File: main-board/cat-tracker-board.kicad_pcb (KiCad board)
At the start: 2 copper layers, 69.5 x 29 mm, 40 parts, among them J1 Conn_01x10, J2 USB_C_Receptacle_USB2.0, J3 Conn_01x03, J4 Conn_01x02, Q1 SI3443DDV-T1-GE3, Q2 Q_PNP_BCE, Q3 Q_NPN_BCE, Q4 SI3443DDV-T1-GE3, Q5 SI3443DDV-T1-GE3, U1 ATSAMD21E18A-A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

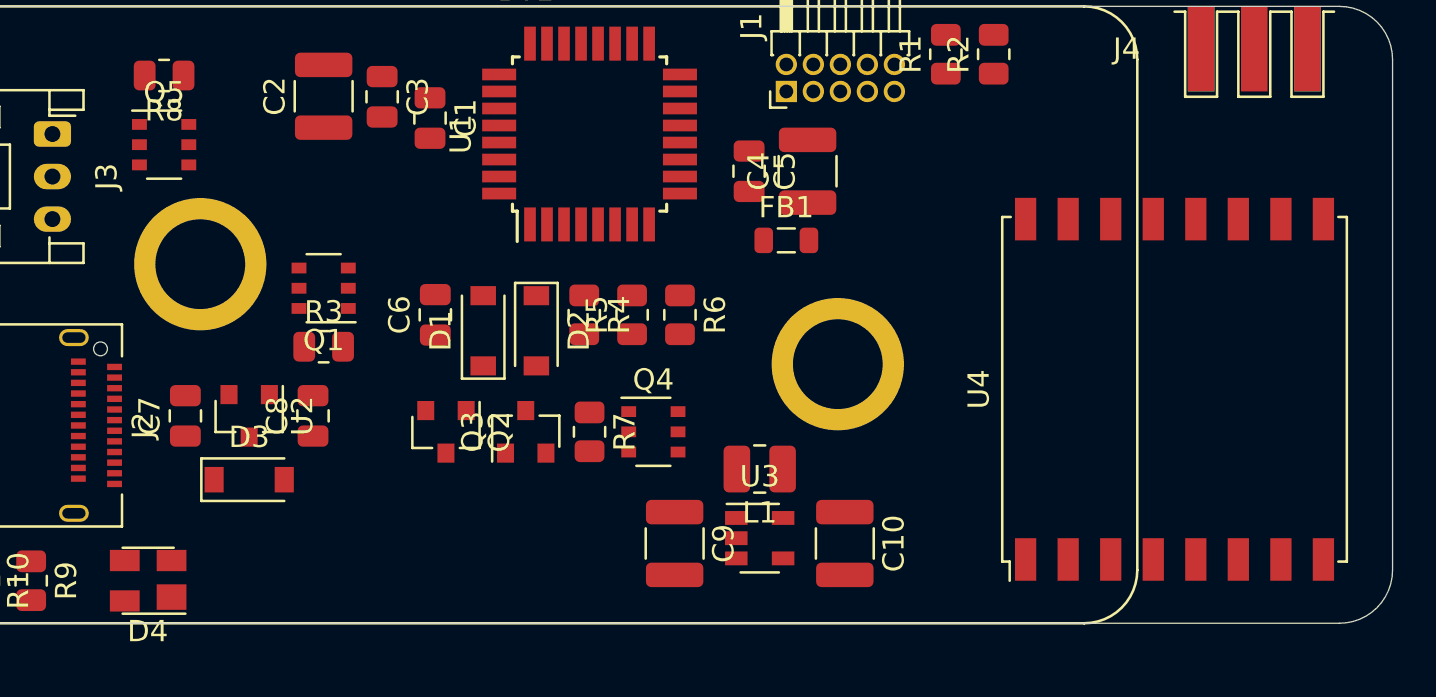
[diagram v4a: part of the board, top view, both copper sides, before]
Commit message: Added zip tie slots.
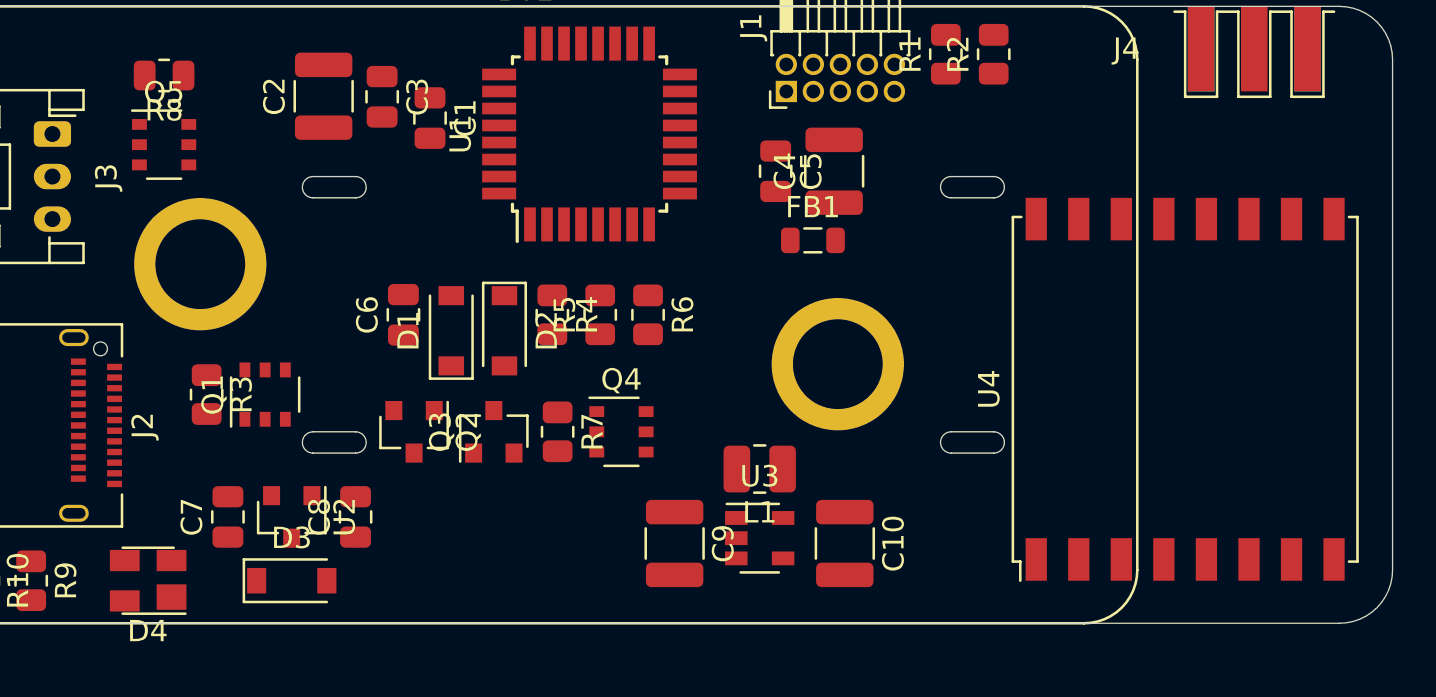
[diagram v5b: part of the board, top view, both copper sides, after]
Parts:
- moved R3 5.94 mm to (13.8, 18.2), turned to 270 degrees
- moved Q1 5.71 mm to (16.5, 18.2), turned to 90 degrees
- moved C7 5.15 mm to (14.8, 24.0)
- moved C8 5.15 mm to (20.8, 24.0)
- moved D3 5.15 mm to (17.8, 27.0)
- moved U2 5.15 mm to (17.8, 24.0)
- moved C6 1.50 mm to (23.0, 14.5)
- moved D1 1.50 mm to (25.2, 15.2)
- moved D2 1.50 mm to (27.8, 15.2)
- moved Q2 1.50 mm to (23.5, 20.0)
- moved Q3 1.50 mm to (27.2, 20.0)
- moved Q4 1.50 mm to (33.2, 20.0)
- moved R4 1.50 mm to (30.0, 14.5)
- moved R5 1.50 mm to (32.2, 14.5)
- moved R6 1.50 mm to (34.5, 14.5)
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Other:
- outline, holes or cut-outs redrawn
- board text added: "CENTER"

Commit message: Started routing.
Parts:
- moved C4 0.85 mm to (44.0, 8.15)
- moved FB1 0.40 mm to (42.2, 11.4)
- turned R8 to 0 degrees
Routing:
- net /USBDP: track 0.00 -> 42.4 mm, vias 0 -> 4
- net /USBDM: track 0.00 -> 38.8 mm, vias 0 -> 3
- net /GPS_EN: track 0.00 -> 34.0 mm, vias 0 -> 3
- net /GPS_TX: track 0.00 -> 33.7 mm
- net /VUSB: track 0.00 -> 30.9 mm, vias 0 -> 3
- net /+3V3: track 0.00 -> 13.8 mm, vias 0 -> 3
- net Net-(J2-PadA5): track 0.00 -> 11.2 mm, vias 0 -> 2
- net /GPS_PWR: track 0.00 -> 10.8 mm
- net Net-(C4-Pad1): track 0.00 -> 10.5 mm
- net Net-(J4-Pad1): track 0.00 -> 10.4 mm
- net Net-(J2-PadB5): track 0.00 -> 8.34 mm, vias 0 -> 2
- net /VBAT: track 0.00 -> 6.63 mm
- net /GND: track 0.00 -> 5.80 mm, vias 0 -> 39
- net Net-(C1-Pad2): track 0.00 -> 3.33 mm
- added copper zone on B.Cu, net /+3V3
- added copper zone on B.Cu, net /GND
- added copper zone on F.Cu, net /GND

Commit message: Finished layout.
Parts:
- turned R3 to 90 degrees
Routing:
- net /VBAT_SW: track 0.00 -> 44.2 mm, vias 0 -> 3
- net /RFM_RESET: track 0.00 -> 38.4 mm, vias 0 -> 2
- net /NSS: track 0.00 -> 34.2 mm, vias 0 -> 2
- net /SCK: track 0.00 -> 31.9 mm, vias 0 -> 2
- net /MISO: track 0.00 -> 31.7 mm, vias 0 -> 2
- net /MOSI: track 0.00 -> 29.7 mm, vias 0 -> 2
- net /SWCLK: track 0.00 -> 29.1 mm, vias 0 -> 1
- net /+3V3: track 13.8 -> 41.6 mm, vias 3 -> 9
- net /RFM_INT: track 0.00 -> 26.0 mm, vias 0 -> 3
- net /nRESET: track 0.00 -> 23.7 mm, vias 0 -> 1
- net /VBAT_LVP: track 0.00 -> 18.7 mm
- net /SWDIO: track 0.00 -> 16.8 mm, vias 0 -> 1
- net Net-(Q2-Pad2): track 0.00 -> 14.3 mm
- net Net-(Q2-Pad3): track 0.00 -> 12.2 mm, vias 0 -> 2
- net Net-(Q2-Pad1): track 0.00 -> 8.45 mm
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
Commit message: Added CPH logo.
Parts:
- added G***: LOGO, colinholzman:CPH-0.25x0.4-F.Mask, B.Cu at (63.8, 15.9)
